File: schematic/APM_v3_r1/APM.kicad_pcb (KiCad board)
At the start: 4 copper layers, 72.5 x 104.5 mm, 90 parts, among them J1 ACM_CTRL, J11 INA219_CONFIG, J12 AUDIO_OUT, J13 Conn_02x36_Odd_Even, J14 periperhals, J15 Conn_02x36_Odd_Even, J16 USB_A, J17 MIDI_DGB, J2 CAN, J29 USB_A, J3 7SDD_CTRL, J30 UART_DEBUG, J4 LCD_display, J5 INTRPT, J7 TDM_PMS_I2C, SW1 WARN_RST, SW2 FAIL_RST, U1 NUCLEO-H753ZI, U13 INA219AxD, U2 CH340G, U38 CH340G, Y1 12MHz, Y7 12MHz

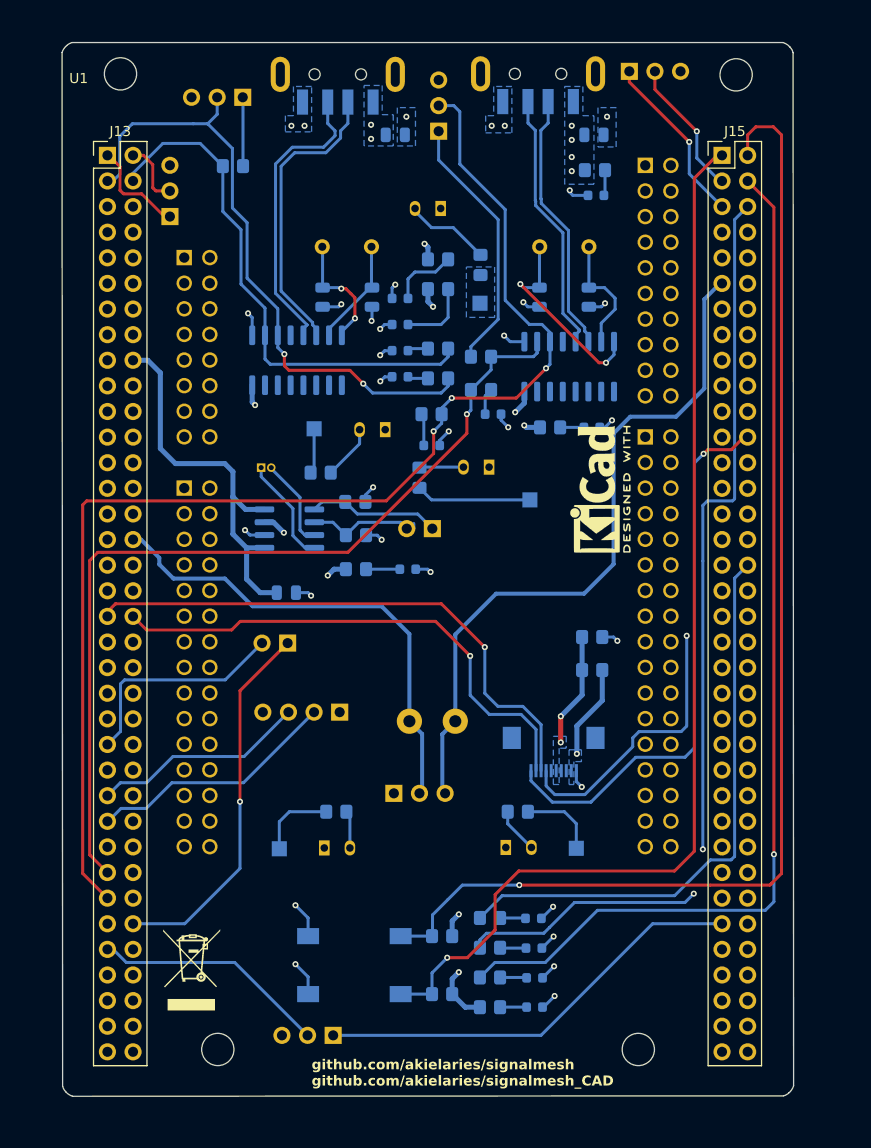
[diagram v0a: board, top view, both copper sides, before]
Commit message: updating top v10. need to get 3v3 APM converged in schematic. routing is tricky right now. the components should be evenly laid out and have the NUCLEO pins be adjusted based on location
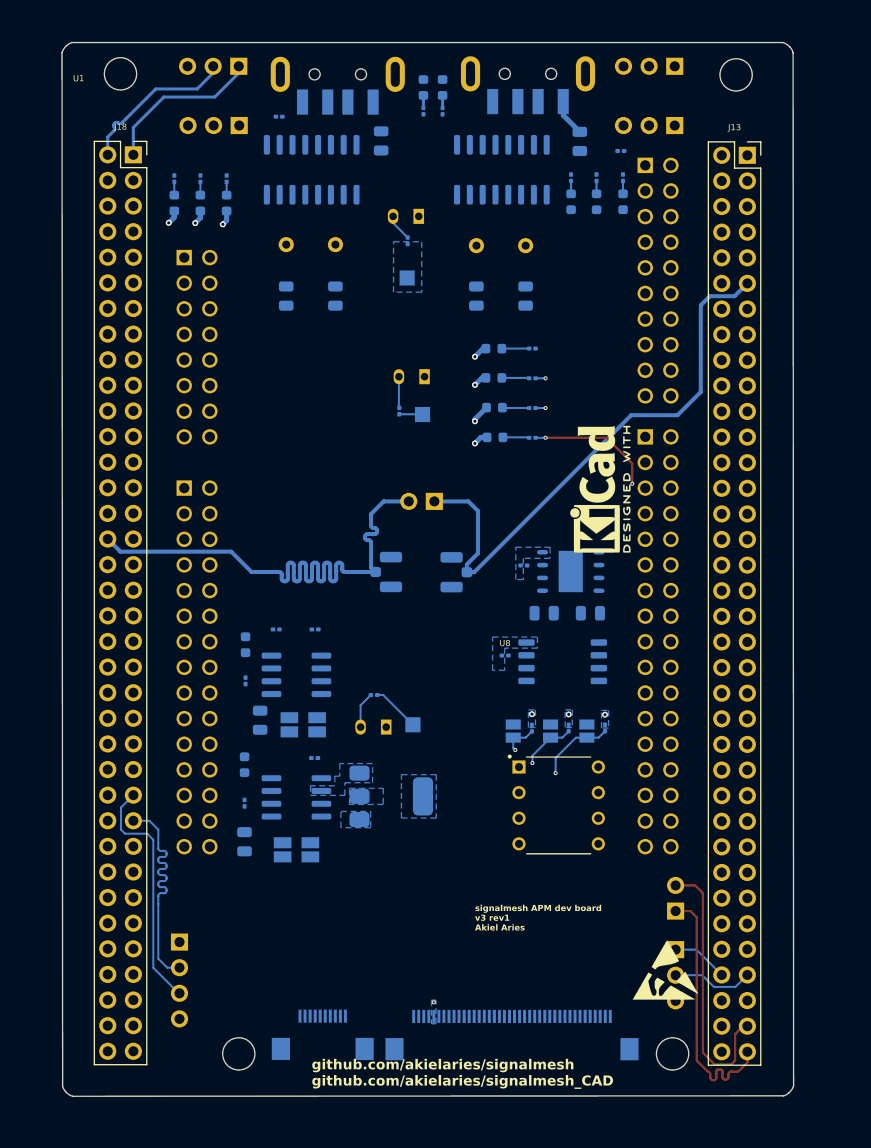
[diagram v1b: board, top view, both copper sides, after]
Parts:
- removed R1, R2: 300, Resistor_SMD:R_0805_2012Metric_Pad1.20x1.40mm_HandSolder
- removed the REF** at (73.3, 143.4)
- removed SW1: WARN_RST, Button_Switch_SMD:SW_SPST_FSMSM
- removed SW2: FAIL_RST, Button_Switch_SMD:SW_SPST_FSMSM
- removed TH1, TH3: 10k, Package_TO_SOT_THT:Heraeus_TO-92-2
- removed TP1: DAC_R_TP, TestPoint:TestPoint_THTPad_D2.5mm_Drill1.2mm
- removed TP2: DAC_L_TP, TestPoint:TestPoint_THTPad_D2.5mm_Drill1.2mm
- removed TP4: THRM_B, TestPoint:TestPoint_Pad_1.5x1.5mm
- removed TP6: THRM_D, TestPoint:TestPoint_Pad_1.5x1.5mm
- added C4: 100nF, Capacitor_SMD:C_0805_2012Metric, B.Cu at (112.8, 108.0)
- added C6: 100nF, Capacitor_SMD:C_0805_2012Metric, B.Cu at (108.3, 108.0)
- added C7: 0.1uf, Capacitor_SMD:C_0805_2012Metric, B.Cu at (78.5, 130.7)
- added D5: LED_PWR, LED_SMD:LED_0603_1608Metric, B.Cu at (78.5, 123.1)
- added J18: Conn_02x36_Odd_Even, Connector_PinSocket_2.54mm:PinSocket_2x36_P2.54mm_Vertical, F.Cu at (67.5, 62.6)
- added JP3: A0, Jumper:SolderJumper-2_P1.3mm_Open_Pad1.0x1.5mm, B.Cu at (105.2, 119.7)
- added JP4: A1, Jumper:SolderJumper-2_P1.3mm_Open_Pad1.0x1.5mm, B.Cu at (108.9, 119.7)
- added JP5: A2, Jumper:SolderJumper-2_P1.3mm_Open_Pad1.0x1.5mm, B.Cu at (112.5, 119.7)
- added R14: 10k, Resistor_SMD:R_0201_0603Metric, B.Cu at (104.4, 112.2)
- added R15: 300, Resistor_SMD:R_0201_0603Metric, B.Cu at (78.5, 126.9)
- added R16: 0.1, Resistor_SMD:R_Shunt_Ohmite_LVK12, B.Cu at (83.7, 131.5)
- added R17: 10k, Resistor_SMD:R_0201_0603Metric, B.Cu at (110.7, 119.4)
- added R18: 10k, Resistor_SMD:R_0201_0603Metric, B.Cu at (114.3, 119.4)
- added U3: LT1963AxST-3.3, Package_TO_SOT_SMD:SOT-223-3_TabPin2, B.Cu at (93.1, 126.2)
- added U4: W25Q128JVS, Package_SO:SOIC-8_5.3x5.3mm_P1.27mm, B.Cu at (110.1, 112.8)
- added U5: MR25H40, Package_DFN_QFN:DFN-S-8-1EP_6x5mm_P1.27mm, B.Cu at (110.9, 103.9)
- added U7: INA219AxD, Package_SO:SOIC-8_3.9x4.9mm_P1.27mm, B.Cu at (83.7, 126.3)
- added U8: 24LC1025-I_P, my_footprints:DIP787W46P254L927H533Q8, F.Cu at (109.7, 127.1)
- J11: value INA219_CONFIG -> DAC_L_PRB; footprint Connector_PinHeader_2.54mm:PinHeader_1x02_P2.54mm_Vertical -> Connector_Coaxial:U.FL_Hirose_U.FL-R-SMT-1_Vertical
- J12: value AUDIO_OUT -> Conn_01x02; footprint Connector_PinHeader_2.54mm:PinHeader_1x03_P2.54mm_Vertical -> Connector_PinHeader_2.54mm:PinHeader_1x02_P2.54mm_Vertical
- J13: footprint Connector_PinHeader_2.54mm:PinHeader_2x36_P2.54mm_Vertical -> Connector_PinSocket_2.54mm:PinSocket_2x36_P2.54mm_Vertical
- J14: value periperhals -> ADC FFC
- J15: value Conn_02x36_Odd_Even -> FPGA FFC; footprint Connector_PinHeader_2.54mm:PinHeader_2x36_P2.54mm_Vertical -> Connector_FFC-FPC:Hirose_FH12-40S-0.5SH_1x40-1MP_P0.50mm_Horizontal; moved to B.Cu
- J7: value TDM_PMS_I2C -> DAC_R_PRB; footprint Connector_PinHeader_1.00mm:PinHeader_1x02_P1.00mm_Vertical -> Connector_Coaxial:U.FL_Hirose_U.FL-R-SMT-1_Vertical
- R10, R11, R12, R13, R26, R28, R30, R39, R40, R41, R5, R53, R6, R7, R8, R88, R89, R9, R90, R91, R92: footprint Resistor_SMD:R_0805_2012Metric_Pad1.20x1.40mm_HandSolder -> Resistor_SMD:R_0201_0603Metric
- R3: value 10k -> 0.1; footprint Resistor_SMD:R_0805_2012Metric_Pad1.20x1.40mm_HandSolder -> Resistor_SMD:R_Shunt_Ohmite_LVK12
- R38: value 300 -> 1.2k; footprint Resistor_SMD:R_0805_2012Metric_Pad1.20x1.40mm_HandSolder -> Resistor_SMD:R_0201_0603Metric
- R4: value 20k -> 10k; footprint Resistor_SMD:R_0805_2012Metric_Pad1.20x1.40mm_HandSolder -> Resistor_SMD:R_0201_0603Metric
- REF**: moved to F.Cu
- moved J15 89.7 mm to (105.1, 149.9), turned to 180 degrees
- moved R38 65.5 mm to (107.1, 81.8), turned to 0 degrees
- moved D15 65.4 mm to (103.3, 81.8), turned to 0 degrees
- moved J13 63.5 mm to (128.4, 62.6)
- moved D16 59.6 mm to (103.3, 84.7), turned to 0 degrees
- moved R39 59.6 mm to (107.1, 84.7), turned to 0 degrees
- moved D17 53.7 mm to (103.3, 87.7), turned to 0 degrees
- moved R40 53.7 mm to (107.1, 87.7), turned to 0 degrees
- moved D18 47.9 mm to (103.4, 90.6), turned to 0 degrees
- moved R41 47.8 mm to (107.1, 90.6), turned to 0 degrees
- moved J5 46.8 mm to (121.3, 137.6), turned to 0 degrees
- moved REF** 40.4 mm to (84.0, 97.6)
- moved J14 36.2 mm to (86.3, 149.8), turned to 180 degrees
- moved J3 35.0 mm to (121.3, 141.4), turned to 180 degrees
- moved R91 31.1 mm to (71.6, 64.9), turned to -90 degrees
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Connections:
- J11 pad 1: Net-(J11-Pin_1) -> /DAC_1-2_L
- J11 pad 2: Net-(J11-Pin_2) -> GND
- J12 pad 1: unconnected-(J12-Pin_1-Pad1) -> /DAC_1-2_L
- J12 pad 2: /APM_DAC_R -> /DAC_1-1_R
- J13 pad 1: /APM_CMD_TX -> /APM_WARN_RST
- J13 pad 11: unconnected-(J13-Pin_11-Pad11) -> /DAC_1-2_L
- J13 pad 12: unconnected-(J13-Pin_12-Pad12) -> /APM_USB_D-
- J13 pad 14: unconnected-(J13-Pin_14-Pad14) -> /APM_USB_D+
- J13 pad 16: 3V3_APM_MCU -> unconnected-(J13-Pin_16-Pad16)
- J13 pad 18: 5V_APM_MCU -> unconnected-(J13-Pin_18-Pad18)
- J13 pad 2: /APM_CMD_RX -> /APM_FAIL_RST
- J13 pad 3: /APM_DBG_TX -> /APM_CAN_RD
- J13 pad 32: /APM_DAC_R -> unconnected-(J13-Pin_32-Pad32)
- J13 pad 37: /POT_3 -> unconnected-(J13-Pin_37-Pad37)
- J13 pad 38: /POT_2 -> unconnected-(J13-Pin_38-Pad38)
- J13 pad 4: /APM_DBG_RX -> unconnected-(J13-Pin_4-Pad4)
- J13 pad 47: /APM_ISR0 -> unconnected-(J13-Pin_47-Pad47)
- J13 pad 5: unconnected-(J13-Pin_5-Pad5) -> /APM_CAN_TD
- J13 pad 51: /APM_I2C1_SCL -> unconnected-(J13-Pin_51-Pad51)
- J13 pad 53: /APM_I2C1_SDA -> unconnected-(J13-Pin_53-Pad53)
- J13 pad 56: unconnected-(J13-Pin_56-Pad56) -> GND
- J13 pad 57: /APM_MIDI_RX -> unconnected-(J13-Pin_57-Pad57)
- J13 pad 59: /APM_MIDI_TX -> unconnected-(J13-Pin_59-Pad59)
- J13 pad 62: /APM_IRQ0 -> unconnected-(J13-Pin_62-Pad62)
- J13 pad 63: /7SDD_CMD_RX -> unconnected-(J13-Pin_63-Pad63)
- J13 pad 65: unconnected-(J13-Pin_65-Pad65) -> /7SDD_CMD_RX
- J13 pad 66: unconnected-(J13-Pin_66-Pad66) -> /7SDD_CMD_TX
- J13 pad 68: unconnected-(J13-Pin_68-Pad68) -> /APM_LED_FAIL
- J13 pad 69: unconnected-(J13-Pin_69-Pad69) -> /APM_ISR0
- J13 pad 70: unconnected-(J13-Pin_70-Pad70) -> /APM_LED_OK
- J13 pad 71: unconnected-(J13-Pin_71-Pad71) -> /APM_IRQ0
- J13 pad 72: unconnected-(J13-Pin_72-Pad72) -> /APM_LED_WARN
- J13 pad 8: GND -> unconnected-(J13-Pin_8-Pad8)
- J13 pad 9: unconnected-(J13-Pin_9-Pad9) -> GND
- J14 pad 1: /POT_1 -> /ADC_1-16_POT_1
- J14 pad 2: /POT_2 -> GND
- J14 pad 3: /POT_3 -> /ADC_1-5_POT_2
- J14 pad 4: /POT_4 -> GND
- J14 pad 5: unconnected-(J14-Pin_5-Pad5) -> /ADC_1-10_POT_3
- J14 pad 6: /3V3_APM -> GND
- J14 pad 7: unconnected-(J14-Pin_7-Pad7) -> /ADC_3-1_POT_4
- J14 pad 8: unconnected-(J14-Pin_8-Pad8) -> GND
- J14 pad 9: 5V_APM -> /3V3_APM
- J15 pad 1: /APM_WARN_RST -> unconnected-(J15-Pin_1-Pad1)
- J15 pad 11: /APM_DAC_L -> unconnected-(J15-Pin_11-Pad11)
- J15 pad 13: unconnected-(J15-Pin_13-Pad13) -> GND
- J15 pad 14: unconnected-(J15-Pin_14-Pad14) -> GND
- J15 pad 2: /APM_FAIL_RST -> unconnected-(J15-Pin_2-Pad2)
- J15 pad 21: unconnected-(J15-Pin_21-Pad21) -> GND
- J15 pad 22: unconnected-(J15-Pin_22-Pad22) -> GND
- J15 pad 23: unconnected-(J15-Pin_23-Pad23) -> GND
- J15 pad 24: /POT_1 -> unconnected-(J15-Pin_24-Pad24)
- J15 pad 29: unconnected-(J15-Pin_29-Pad29) -> GND
- J15 pad 3: /APM_CAN_RD -> GND
- J15 pad 31: unconnected-(J15-Pin_31-Pad31) -> FPGA_3V3_OUT1
- J15 pad 34: /APM_LED_FAIL -> unconnected-(J15-Pin_34-Pad34)
- J15 pad 36: unconnected-(J15-Pin_36-Pad36) -> GND
- J15 pad 37: /POT_4 -> unconnected-(J15-Pin_37-Pad37)
- J15 pad 4: /APM_LED_OK -> FPGA_3V3_OUT1
- J15 pad 5: /APM_CAN_TD -> GND
- J15 pad 6: /APM_LED_WARN -> GND
- J15 pad 7: unconnected-(J15-Pin_7-Pad7) -> GND
- J4 pad 2: /APM_I2C1_SDA -> /APM_I2C2_SDA
- J4 pad 3: /APM_I2C1_SCL -> /APM_I2C2_SCL
- J7 pad 1: /TDM_SCL -> /DAC_1-1_R
- J7 pad 2: /TDM_SDA -> GND
- R26 pad 2: Net-(J11-Pin_2) -> Net-(U13-A0)
- R28 pad 2: Net-(J11-Pin_1) -> Net-(U13-A1)
- R3 pad 1: 5V_APM -> 5V_APM_MCU
- R3 pad 2: /3V3_APM -> Net-(U13-IN+)
- R4 pad 1: /3V3_APM -> GND
- R4 pad 2: GND -> Net-(U7-A1)
- R6 pad 1: Net-(R6-Pad1) -> 3V3_APM
- R6 pad 2: /THRM_D -> Net-(U5-~{HOLD})
- R8 pad 2: /THRM_B -> GND
- U13 pad 1: Net-(J11-Pin_1) -> Net-(U13-A1)
- U13 pad 2: Net-(J11-Pin_2) -> Net-(U13-A0)
- U13 pad 3: /TDM_SDA -> /APM_I2C1_SDA
- U13 pad 4: /TDM_SCL -> /APM_I2C1_SCL
- U13 pad 7: 5V_APM -> Net-(U13-IN-)
- U13 pad 8: 5V_APM_MCU -> Net-(U13-IN+)
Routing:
- net /APM_MIDI_TX: track 126.1 -> 0.00 mm, vias 3 -> 0
- net /APM_FAIL_RST: track 120.8 -> 0.00 mm, vias 1 -> 0
- net /APM_WARN_RST: track 108.7 -> 0.00 mm, vias 1 -> 0
- net /APM_MIDI_RX: track 88.7 -> 0.00 mm, vias 1 -> 0
- net /APM_DAC_L: track 70.1 -> 0.00 mm
- net /APM_DBG_TX: track 63.1 -> 0.00 mm, vias 2 -> 0
- net /POT_3: track 56.0 -> 0.00 mm, vias 1 -> 0
- net /DAC_1-2_L: track 0.00 -> 56.0 mm
- net /DAC_1-1_R: track 0.00 -> 55.7 mm
- net /POT_1: track 54.9 -> 0.00 mm, vias 1 -> 0
- net /APM_DBG_RX: track 52.2 -> 0.00 mm
- net /POT_2: track 51.7 -> 0.00 mm, vias 1 -> 0
- net /APM_DAC_R: track 48.1 -> 0.00 mm
- net GND: track 50.1 -> 10.4 mm, vias 33 -> 11
- net 5V_APM_MCU: track 39.1 -> 0.00 mm
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- added copper zone on B.Cu, net 3V3_APM
- added copper zone on B.Cu, net 3V3_LDO
- removed copper zone on B.Cu, net /3V3_APM
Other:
- board text added: "IRQ"
- board text added: "ISR"
- board text removed: "IRQ0"
- board text removed: "ISR0"

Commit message: i got orientation wrong big time
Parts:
- removed R11, R90: 1k5, Resistor_SMD:R_0201_0603Metric
- R89: value 300 -> 1.2k
- moved G*** 42.4 mm to (84.0, 137.2)
- moved REF** 42.4 mm to (83.2, 139.9)
- moved C5 32.9 mm to (80.0, 85.8)
- moved C7 32.8 mm to (79.9, 98.0)
- moved R3 29.3 mm to (85.2, 89.8)
- moved R16 29.1 mm to (85.2, 102.4)
- moved R26 29.1 mm to (83.2, 80.6)
- moved R28 29.1 mm to (87.0, 80.6)
- moved R4 29.1 mm to (87.0, 93.3)
- moved U13 29.1 mm to (85.2, 85.1)
- moved U3 29.1 mm to (94.5, 97.1)
- moved U7 29.1 mm to (85.2, 97.2)
- moved R30 26.8 mm to (90.4, 90.7)
- moved D7 25.8 mm to (90.4, 88.2)
- moved R15 22.8 mm to (79.8, 104.1)
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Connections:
- J13 pad 12: /APM_USB_D- -> /APM_MIDI_RX
- J13 pad 14: /APM_USB_D+ -> /APM_MIDI_TX
- J13 pad 20: unconnected-(J13-Pin_20-Pad20) -> GND
- J13 pad 21: unconnected-(J13-Pin_21-Pad21) -> /APM_EEPROM_EN
- J13 pad 23: unconnected-(J13-Pin_23-Pad23) -> /APM_MRAM_EN
- J13 pad 25: unconnected-(J13-Pin_25-Pad25) -> /APM_SPIFLASH_EN
- J13 pad 27: unconnected-(J13-Pin_27-Pad27) -> /APM_SPI1_MISO
- J13 pad 29: unconnected-(J13-Pin_29-Pad29) -> /APM_SPI1_MOSI
- J13 pad 31: unconnected-(J13-Pin_31-Pad31) -> /APM_SPI1_SCK
- J13 pad 32: unconnected-(J13-Pin_32-Pad32) -> GND
- J13 pad 33: unconnected-(J13-Pin_33-Pad33) -> /SPIFLASH_CS
- J13 pad 35: unconnected-(J13-Pin_35-Pad35) -> /SPIMRAM_CS
- J13 pad 39: unconnected-(J13-Pin_39-Pad39) -> GND
- J14 pad 9: /3V3_APM -> 3V3_APM
- J17 pad 1: /USB_MIDI_APM/APM_MIDI_TX -> /APM_MIDI_TX
- J17 pad 2: /APM_MIDI_TX -> /APM_MIDI_RX
- J18 pad 47: /APM_SPI1_MOSI -> unconnected-(J18-Pin_47-Pad47)
- J18 pad 57: /APM_MIDI_RX -> unconnected-(J18-Pin_57-Pad57)
- J18 pad 59: /APM_MIDI_TX -> unconnected-(J18-Pin_59-Pad59)
- J18 pad 64: /APM_SPIFLASH_EN -> unconnected-(J18-Pin_64-Pad64)
- J18 pad 65: /APM_SPI1_MISO -> unconnected-(J18-Pin_65-Pad65)
- J18 pad 66: /APM_MRAM_EN -> unconnected-(J18-Pin_66-Pad66)
- J18 pad 68: /APM_EEPROM_EN -> unconnected-(J18-Pin_68-Pad68)
- J18 pad 69: /SPIFLASH_CS -> unconnected-(J18-Pin_69-Pad69)
- J18 pad 71: /SPIMRAM_CS -> unconnected-(J18-Pin_71-Pad71)
- J18 pad 72: /APM_SPI1_SCK -> unconnected-(J18-Pin_72-Pad72)
- J30 pad 1: /USB_debug_APM/APM_DBG_TX -> /APM_DBG_TX
- J30 pad 2: /APM_DBG_TX -> /APM_DBG_RX
- R12 pad 1: /APM_MIDI_RX -> /APM_MIDI_TX
- R13 pad 1: /APM_MIDI_TX -> /APM_MIDI_RX
- R15 pad 2: /3V3_APM -> 3V3_APM
- R16 pad 4: /3V3_APM -> 3V3_APM
- R91 pad 1: /APM_DBG_RX -> /APM_DBG_TX
- R92 pad 1: /APM_DBG_TX -> /APM_DBG_RX
- U2 pad 2: /APM_MIDI_RX -> /APM_MIDI_TX
- U2 pad 3: /APM_MIDI_TX -> /APM_MIDI_RX
- U38 pad 2: /APM_DBG_RX -> /APM_DBG_TX
- U38 pad 3: /APM_DBG_TX -> /APM_DBG_RX
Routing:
- net /APM_MIDI_TX: track 0.00 -> 51.9 mm, vias 0 -> 2
- net /APM_MIDI_RX: track 0.00 -> 51.7 mm, vias 0 -> 2
- net GND: track 10.4 -> 60.3 mm, vias 11 -> 44
- net /APM_DBG_RX: track 0.00 -> 39.8 mm, vias 0 -> 2
- net /APM_DBG_TX: track 0.00 -> 39.5 mm, vias 0 -> 2
- net 3V3_APM: track 0.00 -> 37.4 mm, vias 0 -> 2
- net 5V_APM: track 3.68 -> 40.2 mm, vias 0 -> 11
- net /DAC_1-1_R: track 55.7 -> 23.0 mm
- net 5V_APM_MCU: track 0.00 -> 31.7 mm
- net /DAC_1-2_L: track 56.0 -> 31.8 mm
- net /APM_I2C2_SCL: track 23.9 -> 0.00 mm
- net /APM_I2C2_SDA: track 22.8 -> 0.00 mm
- net /APM_CAN_TD: track 0.00 -> 22.0 mm
- net /APM_CAN_RD: track 0.00 -> 21.9 mm
- net 3V3_LDO: track 0.00 -> 17.9 mm, vias 0 -> 3
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- added copper zone on B.Cu, net /APM_DBG_RX
- added copper zone on B.Cu, net /APM_DBG_TX

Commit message: more progress
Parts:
- moved J4 4.09 mm to (73.2, 144.6), turned to 0 degrees
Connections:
- J13 pad 1: /APM_WARN_RST -> /APM_MIDI_RX
- J13 pad 11: /DAC_1-2_L -> unconnected-(J13-Pin_11-Pad11)
- J13 pad 12: /APM_MIDI_RX -> unconnected-(J13-Pin_12-Pad12)
- J13 pad 14: /APM_MIDI_TX -> unconnected-(J13-Pin_14-Pad14)
- J13 pad 17: unconnected-(J13-Pin_17-Pad17) -> 5V_APM_MCU
- J13 pad 19: unconnected-(J13-Pin_19-Pad19) -> GND
- J13 pad 2: /APM_FAIL_RST -> /APM_MIDI_TX
- J13 pad 21: /APM_EEPROM_EN -> GND
- J13 pad 23: /APM_MRAM_EN -> unconnected-(J13-Pin_23-Pad23)
- J13 pad 25: /APM_SPIFLASH_EN -> /NC
- J13 pad 26: unconnected-(J13-Pin_26-Pad26) -> /NC
- J13 pad 27: /APM_SPI1_MISO -> unconnected-(J13-Pin_27-Pad27)
- J13 pad 28: unconnected-(J13-Pin_28-Pad28) -> /NC
- J13 pad 29: /APM_SPI1_MOSI -> /ADC_1-16_POT_1
- J13 pad 3: /APM_CAN_RD -> /UART5_RX
- J13 pad 30: unconnected-(J13-Pin_30-Pad30) -> /NC
- J13 pad 31: /APM_SPI1_SCK -> /DAC_1-1_R
- J13 pad 32: GND -> unconnected-(J13-Pin_32-Pad32)
- J13 pad 33: /SPIFLASH_CS -> /ADC_1-5_POT_2
- J13 pad 35: /SPIMRAM_CS -> /ADC_1-10_POT_3
- J13 pad 36: unconnected-(J13-Pin_36-Pad36) -> /ADC_3-1_POT_4
- J13 pad 39: GND -> unconnected-(J13-Pin_39-Pad39)
- J13 pad 4: unconnected-(J13-Pin_4-Pad4) -> /UART5_TX
- J13 pad 44: unconnected-(J13-Pin_44-Pad44) -> /7SDD_CMD_TX
- J13 pad 45: unconnected-(J13-Pin_45-Pad45) -> /APM_SPI4_SCK
- J13 pad 46: unconnected-(J13-Pin_46-Pad46) -> /7SDD_CMD_RX
- J13 pad 49: unconnected-(J13-Pin_49-Pad49) -> /APM_SPI4_MISO
- J13 pad 5: /APM_CAN_TD -> unconnected-(J13-Pin_5-Pad5)
- J13 pad 51: unconnected-(J13-Pin_51-Pad51) -> /SPIFLASH_CS
- J13 pad 52: unconnected-(J13-Pin_52-Pad52) -> GND
- J13 pad 53: unconnected-(J13-Pin_53-Pad53) -> /SPIMRAM_CS
- J13 pad 54: unconnected-(J13-Pin_54-Pad54) -> /APM_I2C2_SCL
- J13 pad 55: unconnected-(J13-Pin_55-Pad55) -> /SPIFPGA_CS
- J13 pad 56: GND -> /APM_I2C2_SDA
- J13 pad 61: unconnected-(J13-Pin_61-Pad61) -> GND
- J13 pad 63: unconnected-(J13-Pin_63-Pad63) -> /APM_SPI4_MOSI
- J13 pad 64: unconnected-(J13-Pin_64-Pad64) -> /APM_SPIFLASH_EN
- J13 pad 65: /7SDD_CMD_RX -> /APM_LED_FAIL
- J13 pad 66: /7SDD_CMD_TX -> /APM_MRAM_EN
- J13 pad 67: unconnected-(J13-Pin_67-Pad67) -> /APM_LED_OK
- J13 pad 68: /APM_LED_FAIL -> /APM_EEPROM_EN
- J13 pad 69: /APM_ISR0 -> /APM_LED_WARN
- J13 pad 7: unconnected-(J13-Pin_7-Pad7) -> GND
- J13 pad 70: /APM_LED_OK -> /NC
- J13 pad 71: /APM_IRQ0 -> /APM_ISR0
- J13 pad 72: /APM_LED_WARN -> /APM_IRQ0
- J13 pad 9: GND -> unconnected-(J13-Pin_9-Pad9)
- J14 pad 1: /ADC_1-16_POT_1 -> /ADC_1-2_POT_1
- J14 pad 3: /ADC_1-5_POT_2 -> /ADC_2-2_POT_2
- J14 pad 5: /ADC_1-10_POT_3 -> /ADC_3-5_POT_3
- J14 pad 7: /ADC_3-1_POT_4 -> /ADC_3-6_POT_4
- J15 pad 10: unconnected-(J15-Pin_10-Pad10) -> /SPIFPGA_CS
- J15 pad 8: unconnected-(J15-Pin_8-Pad8) -> /APM_I2C2_SDA
- J15 pad 9: unconnected-(J15-Pin_9-Pad9) -> /APM_I2C2_SCL
- J18 pad 1: /APM_CMD_TX -> unconnected-(J18-Pin_1-Pad1)
- J18 pad 10: unconnected-(J18-Pin_10-Pad10) -> GND
- J18 pad 11: unconnected-(J18-Pin_11-Pad11) -> /APM_CAN_TD
- J18 pad 12: unconnected-(J18-Pin_12-Pad12) -> /DAC_1-2_L
- J18 pad 13: unconnected-(J18-Pin_13-Pad13) -> /APM_CAN_RD
- J18 pad 16: 3V3_APM_MCU -> unconnected-(J18-Pin_16-Pad16)
- J18 pad 17: unconnected-(J18-Pin_17-Pad17) -> /APM_DBG_RX
- J18 pad 18: 5V_APM_MCU -> unconnected-(J18-Pin_18-Pad18)
- J18 pad 2: /APM_CMD_RX -> unconnected-(J18-Pin_2-Pad2)
- J18 pad 3: /APM_DBG_TX -> unconnected-(J18-Pin_3-Pad3)
- J18 pad 30: /ADC_1-16_POT_1 -> unconnected-(J18-Pin_30-Pad30)
- J18 pad 32: /DAC_1-1_R -> unconnected-(J18-Pin_32-Pad32)
- J18 pad 34: /ADC_1-5_POT_2 -> unconnected-(J18-Pin_34-Pad34)
- J18 pad 35: /ADC_3-1_POT_4 -> unconnected-(J18-Pin_35-Pad35)
- J18 pad 36: /ADC_1-10_POT_3 -> unconnected-(J18-Pin_36-Pad36)
- J18 pad 4: /APM_DBG_RX -> /APM_CMD_RX
- J18 pad 44: unconnected-(J18-Pin_44-Pad44) -> /ADC_3-6_POT_4
- J18 pad 51: /APM_I2C2_SCL -> unconnected-(J18-Pin_51-Pad51)
- J18 pad 53: /APM_I2C2_SDA -> unconnected-(J18-Pin_53-Pad53)
- J18 pad 59: unconnected-(J18-Pin_59-Pad59) -> /ADC_1-2_POT_1
- J18 pad 6: unconnected-(J18-Pin_6-Pad6) -> /APM_CMD_TX
- J18 pad 60: unconnected-(J18-Pin_60-Pad60) -> /ADC_3-5_POT_3
- J18 pad 61: unconnected-(J18-Pin_61-Pad61) -> /ADC_2-2_POT_2
- J18 pad 66: unconnected-(J18-Pin_66-Pad66) -> GND
- J18 pad 8: GND -> unconnected-(J18-Pin_8-Pad8)
- J18 pad 9: unconnected-(J18-Pin_9-Pad9) -> /APM_DBG_TX
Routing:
- net /APM_I2C2_SCL: track 0.00 -> 69.2 mm, vias 0 -> 1
- net /APM_I2C2_SDA: track 0.00 -> 69.0 mm, vias 0 -> 1
- net /APM_CAN_TD: track 22.0 -> 0.00 mm
- net /APM_CAN_RD: track 21.9 -> 0.00 mm
- net /DAC_1-2_L: track 31.8 -> 10.2 mm
- net /APM_DBG_TX: track 39.5 -> 18.7 mm
- net GND: track 60.3 -> 73.4 mm, vias 44 -> 49
- net /DAC_1-1_R: track 23.0 -> 10.2 mm
- net 5V_APM_MCU: track 31.7 -> 19.8 mm
- net /APM_DBG_RX: track 39.8 -> 29.6 mm
- net /APM_MIDI_RX: track 51.7 -> 42.0 mm
- net /APM_CMD_RX: track 15.5 -> 6.65 mm
- net /APM_MIDI_TX: track 51.9 -> 43.2 mm
- net /APM_IRQ0: track 26.4 -> 19.4 mm, vias 0 -> 1
- net /APM_CMD_TX: track 15.4 -> 8.71 mm
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
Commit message: more routing
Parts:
- added D19: FPGA_PWR, LED_SMD:LED_0603_1608Metric, B.Cu at (99.8, 140.2)
- added R42: 300, Resistor_SMD:R_0201_0603Metric, B.Cu at (99.8, 142.7)
- moved J11 7.01 mm to (90.0, 114.9), turned to 0 degrees
- moved J7 6.90 mm to (96.9, 114.9), turned to 180 degrees
- moved J12 2.55 mm to (92.2, 107.8), turned to -90 degrees
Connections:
- J15 pad 10: /SPIFPGA_CS -> unconnected-(J15-Pin_10-Pad10)
- J15 pad 11: unconnected-(J15-Pin_11-Pad11) -> GND
- J15 pad 12: unconnected-(J15-Pin_12-Pad12) -> /APM_SPI1_CLK
- J15 pad 15: unconnected-(J15-Pin_15-Pad15) -> /APM_SPI1_MISO
- J15 pad 16: unconnected-(J15-Pin_16-Pad16) -> /APM_SPI1_MOSI
- J15 pad 17: unconnected-(J15-Pin_17-Pad17) -> /APM_SPI1_CS
- J15 pad 25: unconnected-(J15-Pin_25-Pad25) -> /APM_FPGA_UART_TX
- J15 pad 26: unconnected-(J15-Pin_26-Pad26) -> /APM_FPGA_UART_RX
- J15 pad 27: unconnected-(J15-Pin_27-Pad27) -> GND
- J15 pad 28: unconnected-(J15-Pin_28-Pad28) -> /QSPI_NCS
- J15 pad 30: unconnected-(J15-Pin_30-Pad30) -> /GCLKT_1
- J15 pad 32: unconnected-(J15-Pin_32-Pad32) -> GND
- J15 pad 33: unconnected-(J15-Pin_33-Pad33) -> /QSPI_IO_3
- J15 pad 34: unconnected-(J15-Pin_34-Pad34) -> /QSPI_IO_2
- J15 pad 38: unconnected-(J15-Pin_38-Pad38) -> GND
- J15 pad 39: unconnected-(J15-Pin_39-Pad39) -> /QSPI_IO_1
- J15 pad 40: unconnected-(J15-Pin_40-Pad40) -> /QSPI_IO_0
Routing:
- net 3V3_APM: track 39.3 -> 112.4 mm, vias 2 -> 6
- net /APM_CAN_TD: track 0.00 -> 63.4 mm, vias 0 -> 1
- net /APM_CAN_RD: track 0.00 -> 62.9 mm
- net /APM_MRAM_EN: track 0.00 -> 58.7 mm
- net /DAC_1-2_L: track 10.2 -> 68.7 mm
- net /DAC_1-1_R: track 10.2 -> 68.6 mm
- net /SPIMRAM_CS: track 0.00 -> 47.7 mm, vias 0 -> 1
- net /APM_SPIFLASH_EN: track 0.00 -> 45.2 mm, vias 0 -> 3
- net 5V_APM_MCU: track 19.8 -> 64.6 mm, vias 0 -> 1
- net /ADC_3-6_POT_4: track 0.00 -> 42.2 mm
- net /APM_EEPROM_EN: track 0.00 -> 41.1 mm
- net /SPIFLASH_CS: track 0.00 -> 38.0 mm, vias 0 -> 1
- net /ADC_1-2_POT_1: track 0.00 -> 29.4 mm, vias 0 -> 1
- net /ADC_3-5_POT_3: track 0.00 -> 28.9 mm, vias 0 -> 1
- net GND: track 73.4 -> 100.7 mm, vias 49 -> 64
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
